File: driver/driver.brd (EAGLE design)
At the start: 6.9 x 7 mm, 38 parts, among them IC1 7805TV, IC2 7806T, Q1 IRF530, Q10 TIP31C, Q2 IRF9530, Q3 IRF530, Q4 IRF9530, Q5 IRF530, Q6 IRF9530, Q7 IRF530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

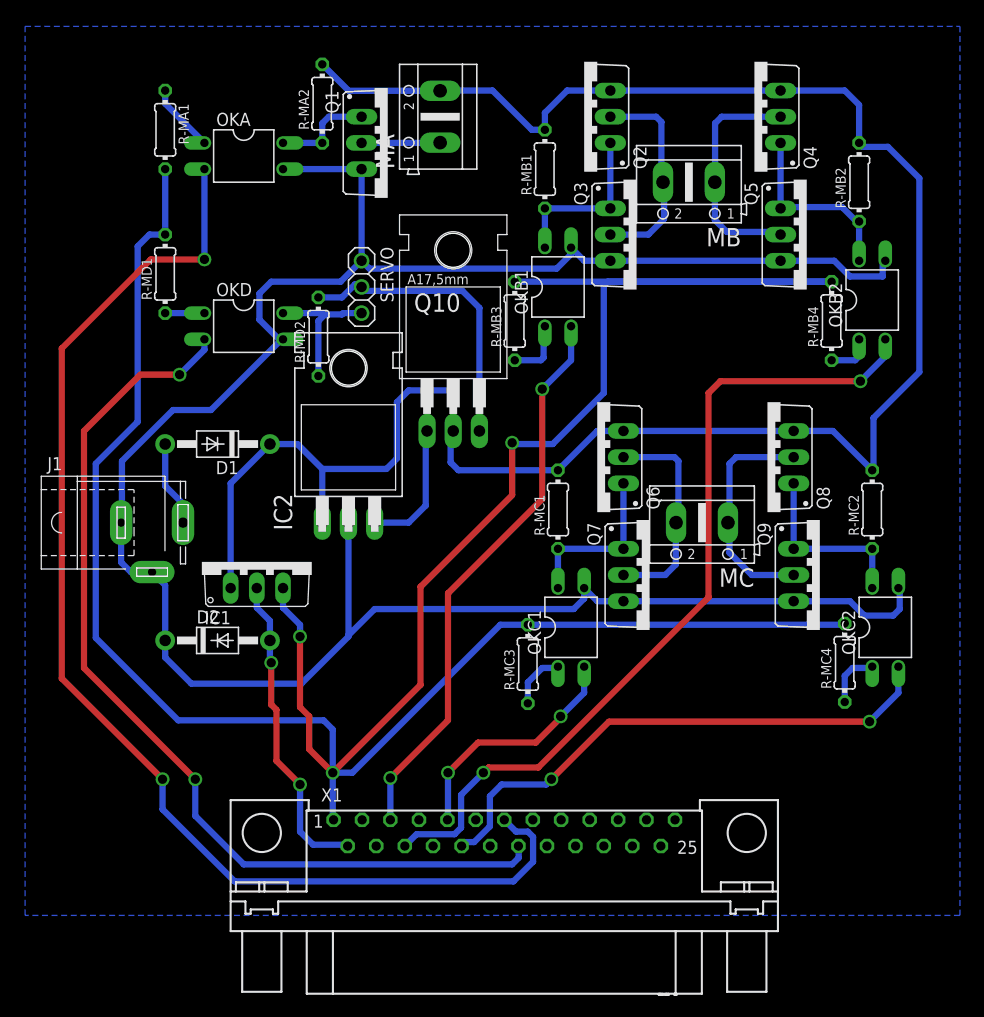
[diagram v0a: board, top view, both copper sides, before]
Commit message: Add egde-line on top layer
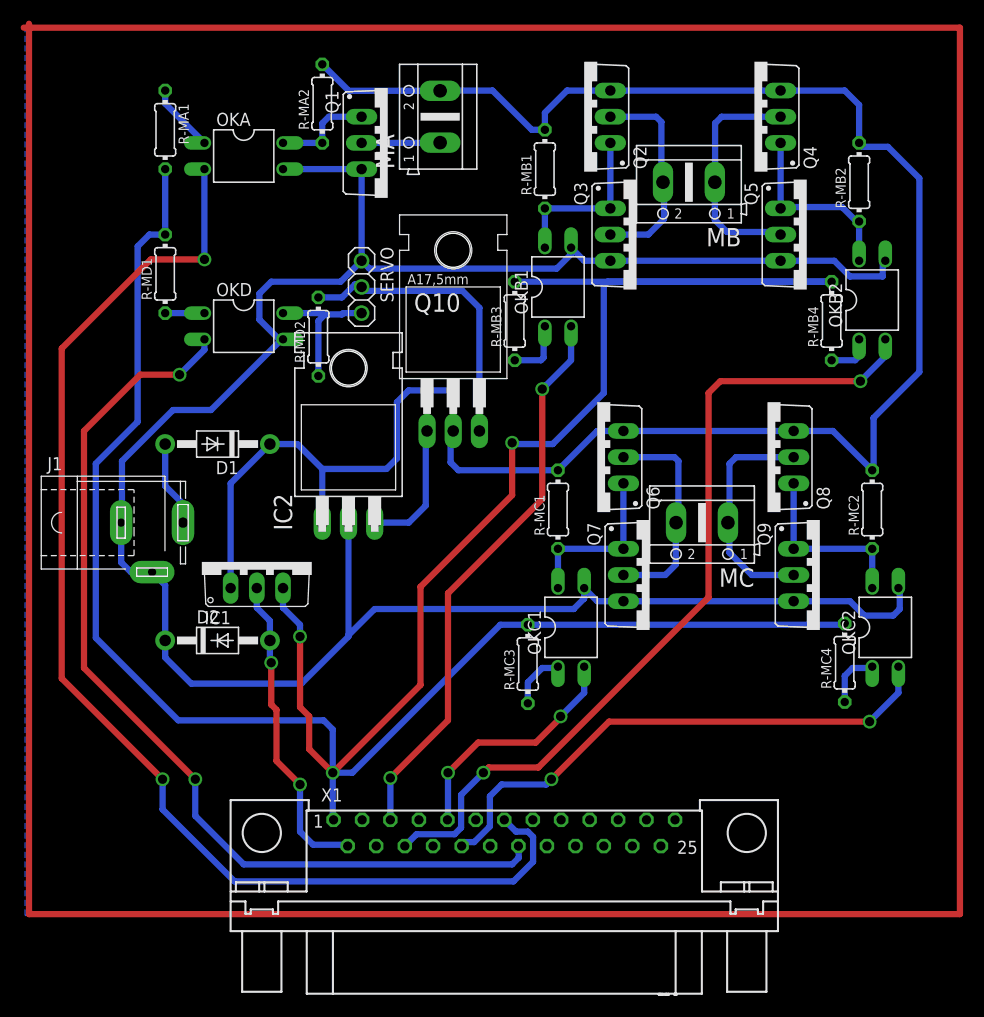
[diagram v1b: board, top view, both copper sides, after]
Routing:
- net N$20: track 0.00 -> 353.4 mm
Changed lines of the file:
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@@
 <layer number="17" name="Pads" color="2" fill="1" visible="yes" active="yes"/>
 <layer number="18" name="Vias" color="14" fill="1" visible="yes" active="yes"/>
-<layer number="19" name="Unrouted" color="6" fill="1" visible="yes" active="yes"/>
-<layer number="20" name="Dimension" color="15" fill="1" visible="yes" active="yes"/>
-<layer number="21" name="tPlace" color="7" fill="1" visible="yes" active="yes"/>
-<layer number="22" name="bPlace" color="7" fill="1" visible="yes" active="yes"/>
-<layer number="23" name="tOrigins" color="15" fill="1" visible="yes" active="yes"/>
-<layer number="24" name="bOrigins" color="15" fill="1" visible="yes" active="yes"/>
+<layer number="19" name="Unrouted" color="6" fill="1" visible="no" active="yes"/>
+<layer number="20" name="Dimension" color="15" fill="1" visible="no" active="yes"/>
+<layer number="21" name="tPlace" color="7" fill="1" visible="no" active="yes"/>
+<layer number="22" name="bPlace" color="7" fill="1" visible="no" active="yes"/>
+<layer number="23" name="tOrigins" color="15" fill="1" visible="no" active="yes"/>
+<layer number="24" name="bOrigins" color="15" fill="1" visible="no" active="yes"/>
 <layer number="25" name="tNames" color="7" fill="1" visible="no" active="yes"/>
 <layer number="26" name="bNames" color="7" fill="1" visible="no" active="yes"/>
@@
 </polygon>
 </signal>
+<signal name="N$20">
+<wire x1="-7.366" y1="81.026" x2="83.439" y2="81.026" width="0.6096" layer="1"/>
+<wire x1="83.439" y1="81.026" x2="83.439" y2="-4.953" width="0.6096" layer="1"/>
+<wire x1="83.439" y1="-4.953" x2="-6.858" y2="-4.953" width="0.6096" layer="1"/>
+<wire x1="-6.858" y1="-4.953" x2="-6.858" y2="81.407" width="0.6096" layer="1"/>
+</signal>
 </signals>
